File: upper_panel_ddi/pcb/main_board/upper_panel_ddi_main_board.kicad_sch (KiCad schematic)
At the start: 9 parts, among them J1 ROW0, J2 ROW1, J3 ROW2, J4 ROW3, J5 ROW4, J6 ROW5, J7 ROW6, J8 ROW7

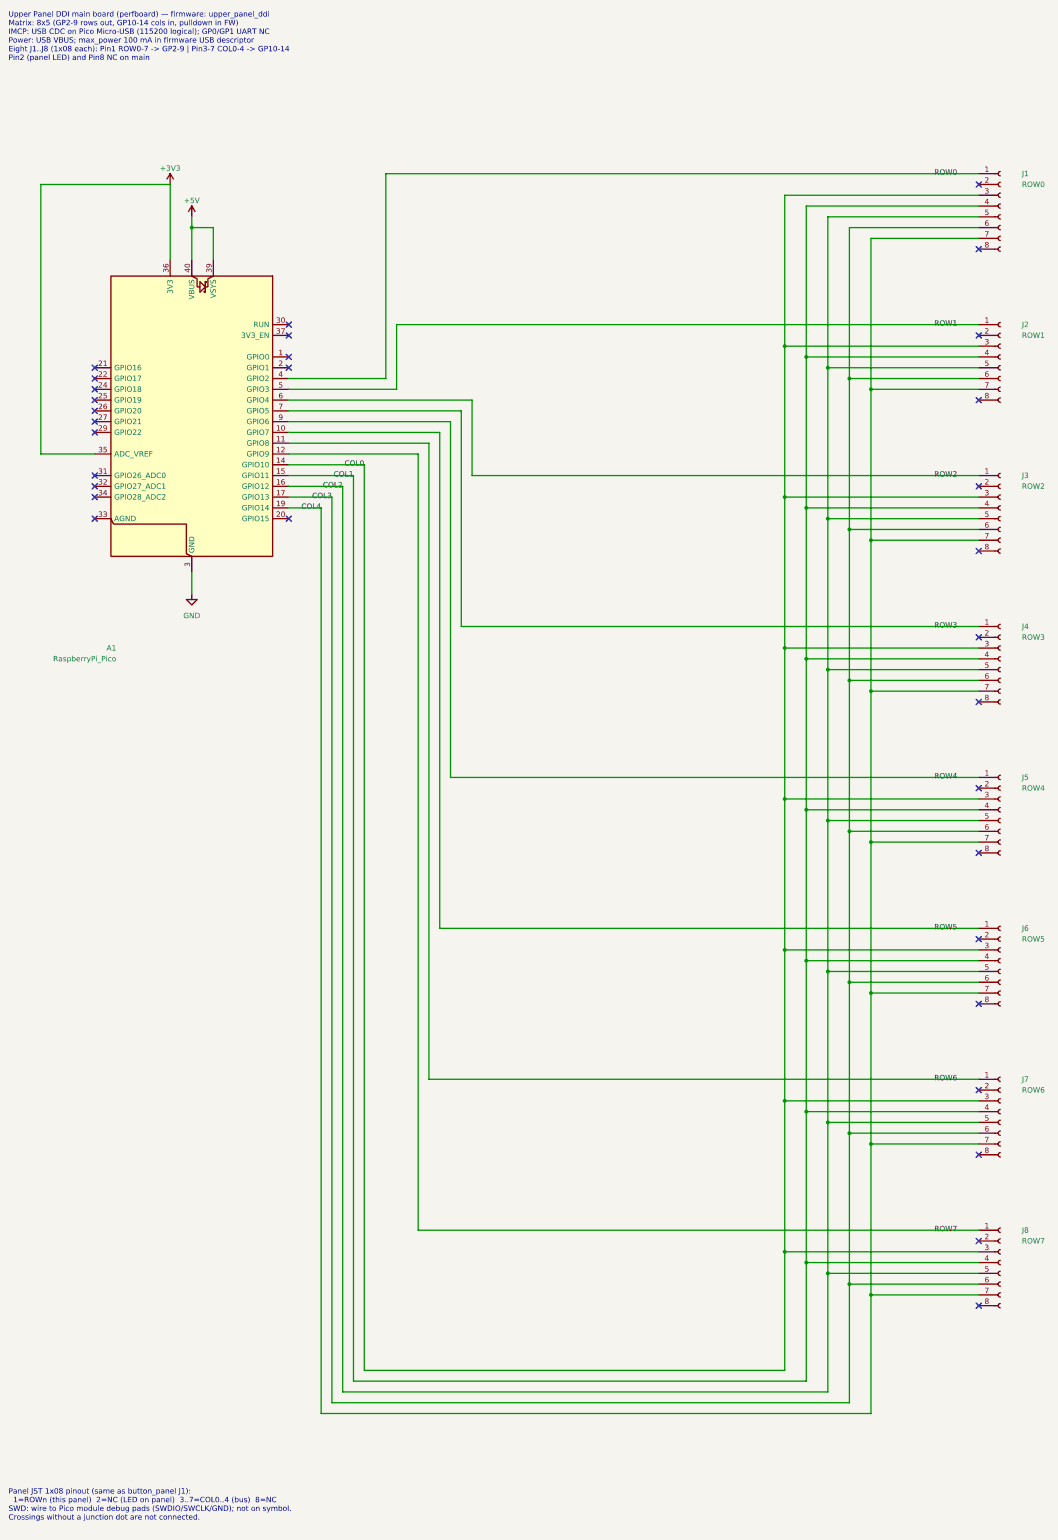
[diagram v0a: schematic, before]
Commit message: fix(hardware): use six-pin main board panel connectors
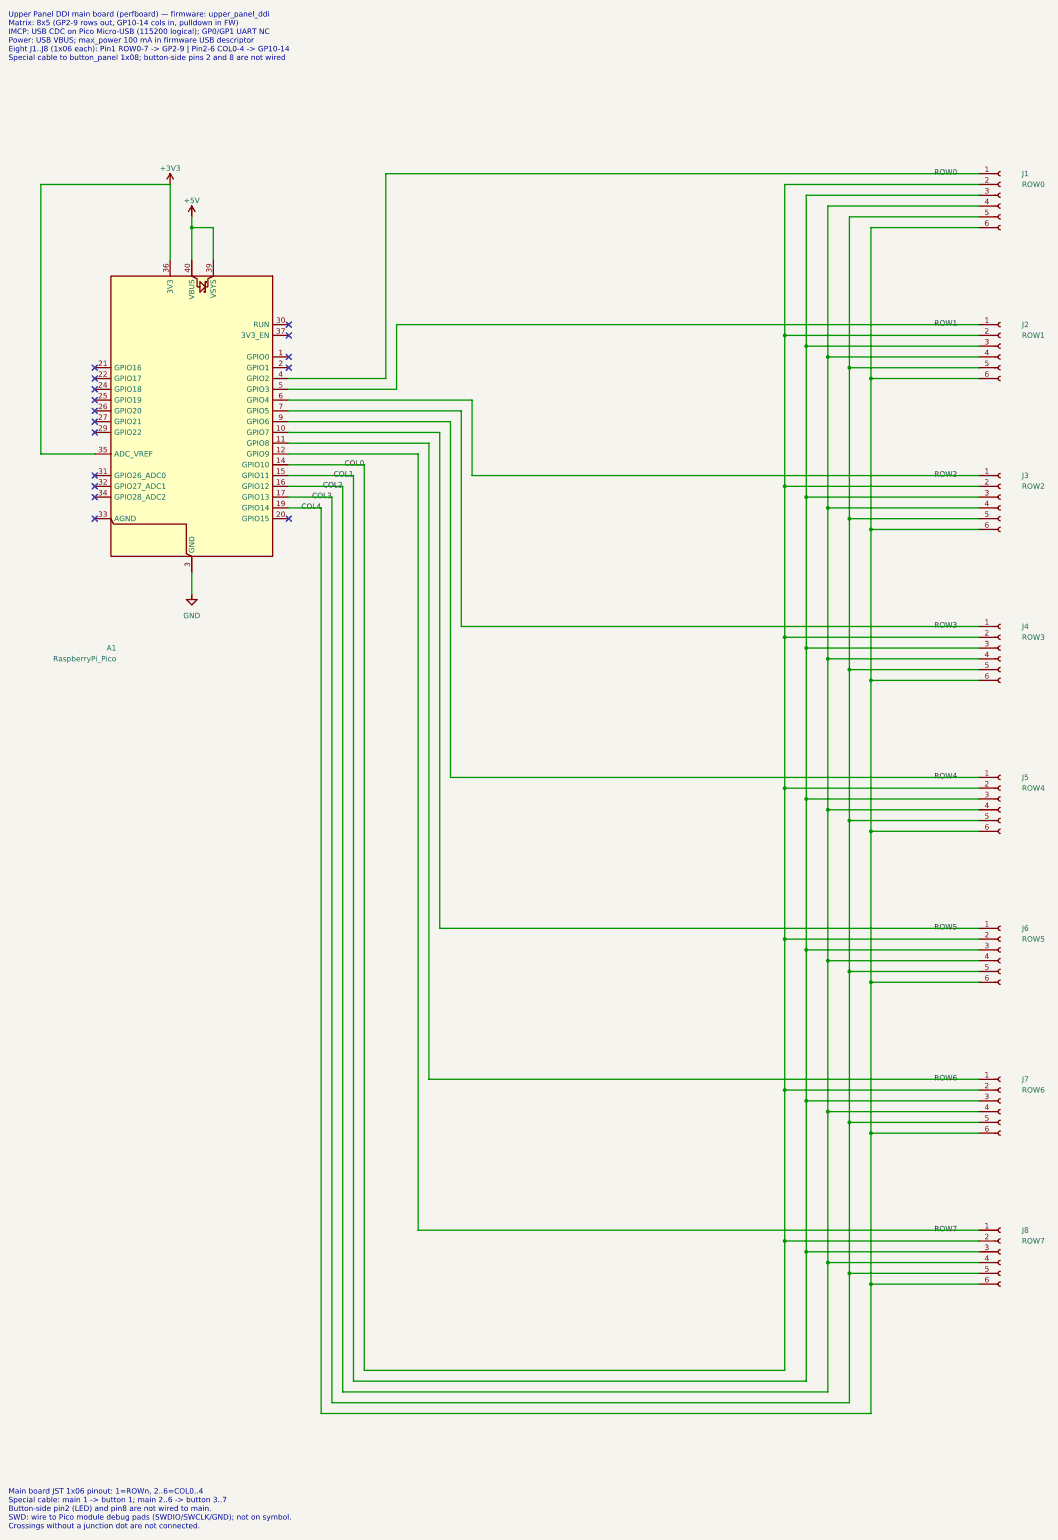
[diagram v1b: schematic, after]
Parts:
- J1, J2, J3, J4, J5, J6, J7, J8: footprint Connector_JST:JST_ZH_B8B-ZR_1x08_P1.50mm_Vertical -> Connector_JST:JST_ZH_B6B-ZR_1x06_P1.50mm_Vertical; symbol Connector:Conn_01x08_Socket -> Connector:Conn_01x06_Socket
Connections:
- net COL0: now also J1.2 (Pin_2), J2.2 (Pin_2), J3.2 (Pin_2), J4.2 (Pin_2), J5.2 (Pin_2), J6.2 (Pin_2), J7.2 (Pin_2), J8.2 (Pin_2); no longer J1.3 (Pin_3), J2.3 (Pin_3), J3.3 (Pin_3), J4.3 (Pin_3), J5.3 (Pin_3), J6.3 (Pin_3), J7.3 (Pin_3), J8.3 (Pin_3)
- net COL1: now also J1.3 (Pin_3), J2.3 (Pin_3), J3.3 (Pin_3), J4.3 (Pin_3), J5.3 (Pin_3), J6.3 (Pin_3), J7.3 (Pin_3), J8.3 (Pin_3); no longer J1.4 (Pin_4), J2.4 (Pin_4), J3.4 (Pin_4), J4.4 (Pin_4), J5.4 (Pin_4), J6.4 (Pin_4), J7.4 (Pin_4), J8.4 (Pin_4)
- net COL2: now also J1.4 (Pin_4), J2.4 (Pin_4), J3.4 (Pin_4), J4.4 (Pin_4), J5.4 (Pin_4), J6.4 (Pin_4), J7.4 (Pin_4), J8.4 (Pin_4); no longer J1.5 (Pin_5), J2.5 (Pin_5), J3.5 (Pin_5), J4.5 (Pin_5), J5.5 (Pin_5), J6.5 (Pin_5), J7.5 (Pin_5), J8.5 (Pin_5)
- net COL3: now also J1.5 (Pin_5), J2.5 (Pin_5), J3.5 (Pin_5), J4.5 (Pin_5), J5.5 (Pin_5), J6.5 (Pin_5), J7.5 (Pin_5), J8.5 (Pin_5); no longer J1.6 (Pin_6), J2.6 (Pin_6), J3.6 (Pin_6), J4.6 (Pin_6), J5.6 (Pin_6), J6.6 (Pin_6), J7.6 (Pin_6), J8.6 (Pin_6)
- net COL4: now also J1.6 (Pin_6), J2.6 (Pin_6), J3.6 (Pin_6), J4.6 (Pin_6), J5.6 (Pin_6), J6.6 (Pin_6), J7.6 (Pin_6), J8.6 (Pin_6); no longer J1.7 (Pin_7), J2.7 (Pin_7), J3.7 (Pin_7), J4.7 (Pin_7), J5.7 (Pin_7), J6.7 (Pin_7), J7.7 (Pin_7), J8.7 (Pin_7)
- no-connect marks 32 -> 16
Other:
- note added: "Main board JST 1x06 pinout: 1=ROWn, 2..6=COL0..4 Special cable: main 1 -> button 1; main 2..6 -> button 3..7 Button-side pin2 (LED) and pin8 are not wired to main. SWD: wire to Pico module debug pads (SWDIO/SWCLK/GND); not on symbol. Crossings without a junction dot are not connected."
- note added: "Upper Panel DDI main board (perfboard) — firmware: upper_panel_ddi Matrix: 8x5 (GP2-9 rows out, GP10-14 cols in, pulldown in FW) IMCP: USB CDC on Pico Micro-USB (115200 logical); GP0/GP1 UART NC Power: USB VBUS; max_power 100 mA in firmware USB descriptor Eight J1..J8 (1x06 each): Pin1 ROW0-7 -> GP2-9 | Pin2-6 COL0-4 -> GP10-14 Special cable to button_panel 1x08; button-side pins 2 and 8 are not 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"
- note removed: "Panel JST 1x08 pinout (same as button_panel J1): 1=ROWn (this panel) 2=NC (LED on panel) 3..7=COL0..4 (bus) 8=NC SWD: wire to Pico module debug pads (SWDIO/SWCLK/GND); not on symbol. Crossings without a junction dot are not connected."
- note removed: "Upper Panel DDI main board (perfboard) — firmware: upper_panel_ddi Matrix: 8x5 (GP2-9 rows out, GP10-14 cols in, pulldown in FW) IMCP: USB CDC on Pico Micro-USB (115200 logical); GP0/GP1 UART NC Power: USB VBUS; max_power 100 mA in firmware USB descriptor Eight J1..J8 (1x08 each): Pin1 ROW0-7 -> GP2-9 | Pin3-7 COL0-4 -> GP10-14 Pin2 (panel LED) and Pin8 NC on main"

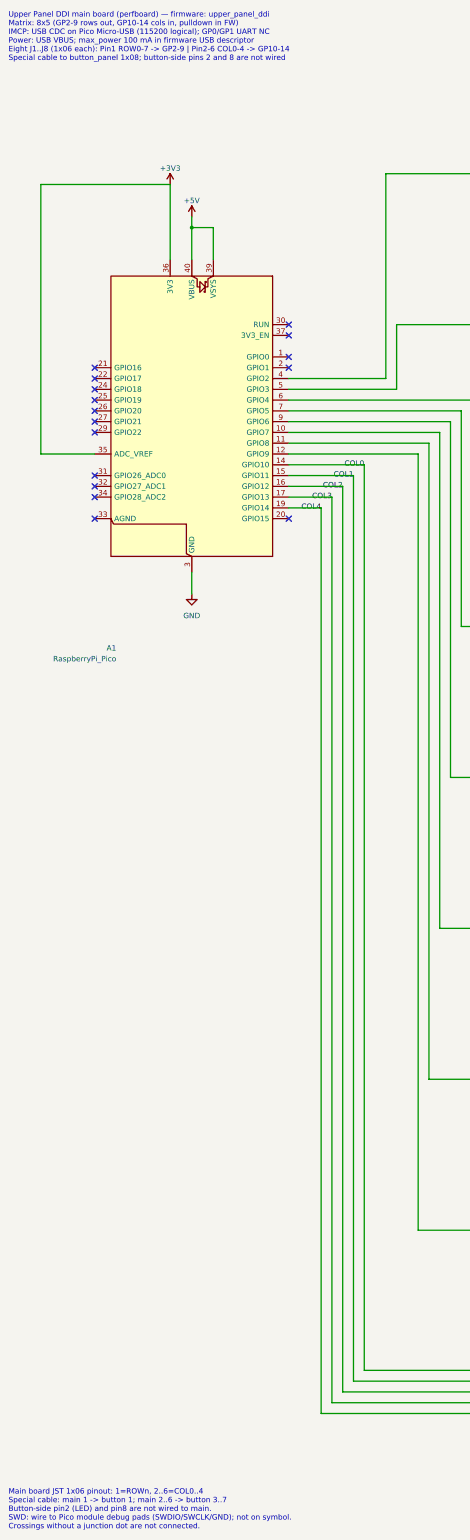
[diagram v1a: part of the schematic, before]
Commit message: fix(hardware): correct button panel row cable mapping
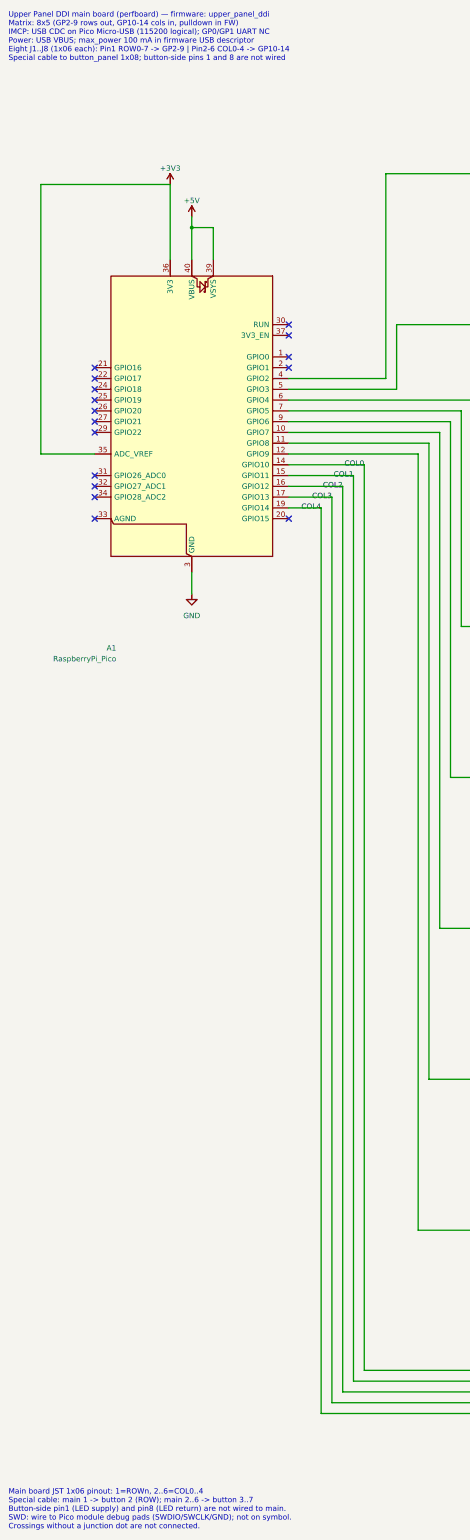
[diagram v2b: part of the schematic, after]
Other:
- note added: "Main board JST 1x06 pinout: 1=ROWn, 2..6=COL0..4 Special cable: main 1 -> button 2 (ROW); main 2..6 -> button 3..7 Button-side pin1 (LED supply) and pin8 (LED return) are not wired to main. SWD: wire to Pico module debug pads (SWDIO/SWCLK/GND); not on symbol. Crossings without a junction dot are not connected."
- note added: "Upper Panel DDI main board (perfboard) — firmware: upper_panel_ddi Matrix: 8x5 (GP2-9 rows out, GP10-14 cols in, pulldown in FW) IMCP: USB CDC on Pico Micro-USB (115200 logical); GP0/GP1 UART NC Power: USB VBUS; max_power 100 mA in firmware USB descriptor Eight J1..J8 (1x06 each): Pin1 ROW0-7 -> GP2-9 | Pin2-6 COL0-4 -> GP10-14 Special cable to button_panel 1x08; button-side pins 1 and 8 are not 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"
- note removed: "Main board JST 1x06 pinout: 1=ROWn, 2..6=COL0..4 Special cable: main 1 -> button 1; main 2..6 -> button 3..7 Button-side pin2 (LED) and pin8 are not wired to main. SWD: wire to Pico module debug pads (SWDIO/SWCLK/GND); not on symbol. Crossings without a junction dot are not connected."
- note removed: "Upper Panel DDI main board (perfboard) — firmware: upper_panel_ddi Matrix: 8x5 (GP2-9 rows out, GP10-14 cols in, pulldown in FW) IMCP: USB CDC on Pico Micro-USB (115200 logical); GP0/GP1 UART NC Power: USB VBUS; max_power 100 mA in firmware USB descriptor Eight J1..J8 (1x06 each): Pin1 ROW0-7 -> GP2-9 | Pin2-6 COL0-4 -> GP10-14 Special cable to button_panel 1x08; button-side pins 2 and 8 are not 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"
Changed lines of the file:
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@@
 	(generator_version "10.0")
 	(paper "A3" portrait)
-	(text "Main board JST 1x06 pinout: 1=ROWn, 2..6=COL0..4\nSpecial cable: main 1 -> button 1; main 2..6 -> button 3..7\nButton-side pin2 (LED) and pin8 are not wired to main.\nSWD: wire to Pico module debug pads (SWDIO/SWCLK/GND); not on symbol.\nCrossings without a junction dot are not connected."
+	(text "Main board JST 1x06 pinout: 1=ROWn, 2..6=COL0..4\nSpecial cable: main 1 -> button 2 (ROW); main 2..6 -> button 3..7\nButton-side pin1 (LED supply) and pin8 (LED return) are not wired to main.\nSWD: wire to Pico module debug pads (SWDIO/SWCLK/GND); not on symbol.\nCrossings without a junction dot are not connected."
 		(exclude_from_sim yes)
 		(at 20.32 363.22 0)
@@
 		)
 	)
-	(text "Upper Panel DDI main board (perfboard) — firmware: upper_panel_ddi\nMatrix: 8x5 (GP2-9 rows out, GP10-14 cols in, pulldown in FW)\nIMCP: USB CDC on Pico Micro-USB (115200 logical); GP0/GP1 UART NC\nPower: USB VBUS; max_power 100 mA in firmware USB descriptor\nEight J1..J8 (1x06 each): Pin1 ROW0-7 -> GP2-9 | Pin2-6 COL0-4 -> GP10-14\nSpecial cable to button_panel 1x08; button-side pins 2 and 8 are not wired"
+	(text "Upper Panel DDI main board (perfboard) — firmware: upper_panel_ddi\nMatrix: 8x5 (GP2-9 rows out, GP10-14 cols in, pulldown in FW)\nIMCP: USB CDC on Pico Micro-USB (115200 logical); GP0/GP1 UART NC\nPower: USB VBUS; max_power 100 mA in firmware USB descriptor\nEight J1..J8 (1x06 each): Pin1 ROW0-7 -> GP2-9 | Pin2-6 COL0-4 -> GP10-14\nSpecial cable to button_panel 1x08; button-side pins 1 and 8 are not wired"
 		(exclude_from_sim yes)
 		(at 20.32 15.24 0)
